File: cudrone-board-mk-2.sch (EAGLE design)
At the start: 144 parts, among them U1 EDISON_CONNECTOR_FULLMOUNTING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, U10 A2235-H, U11 FTS31XS-U, U12 BNO055, U13 DSPIC33EP512MU810-X_PF, U2 FTS31XS-U, U4 TPS62065, U5 USD-SOCKETNEW, U6 TXB0108, U8 PCA9306, U9 PCA9306

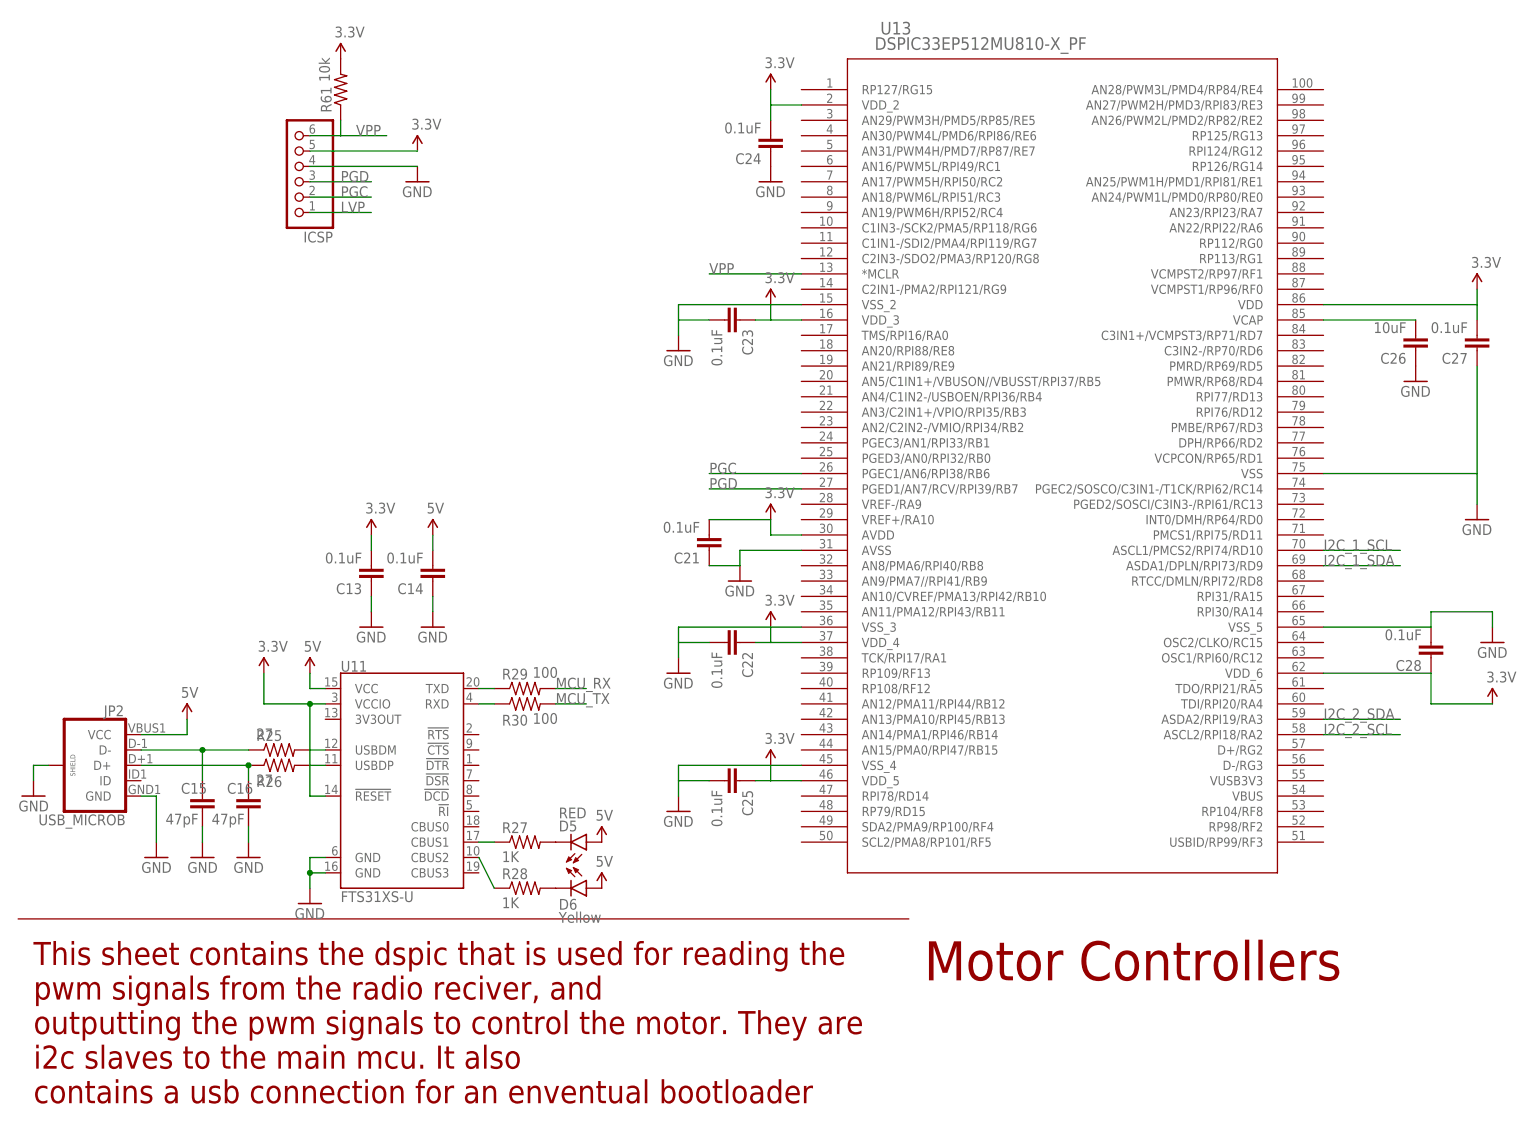
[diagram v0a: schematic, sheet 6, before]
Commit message: Made a few modifications in preparation of assigning pins on mcu
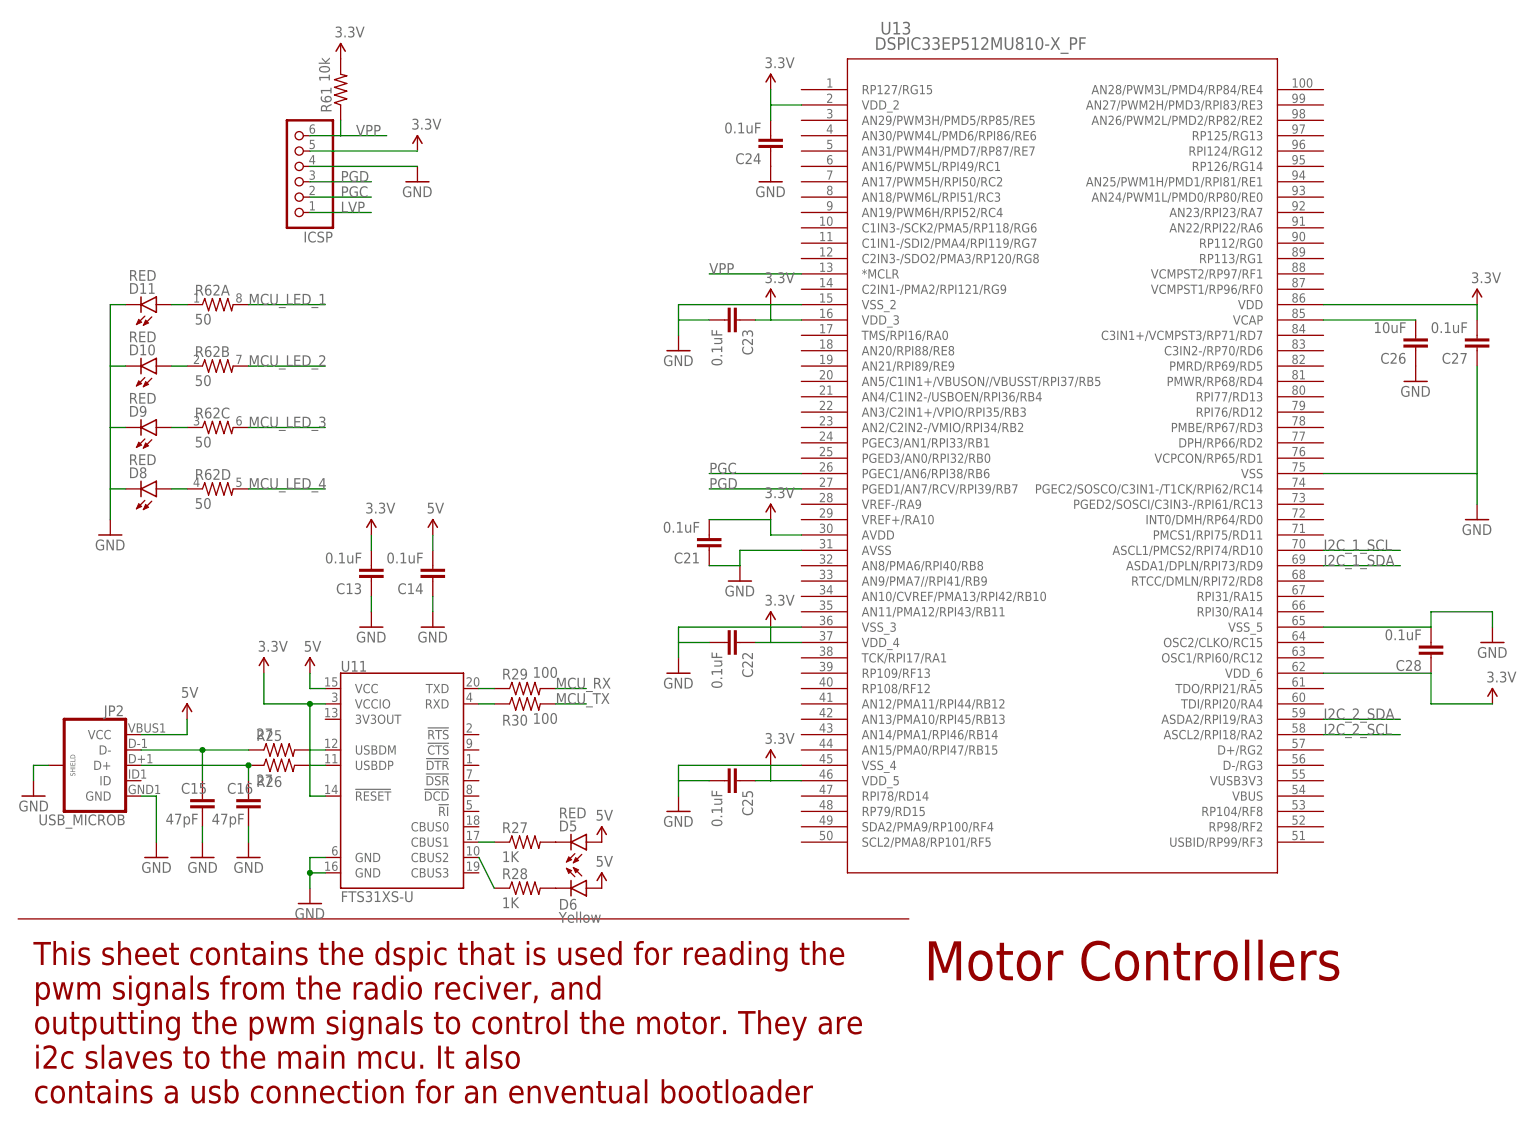
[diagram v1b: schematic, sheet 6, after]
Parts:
- added D10, D11, D8, D9: RED, SparkFun-LED:LED-RED0603
- added R62: 50, SparkFun-Passives:RESISTOR-ARRAY0603-ARV
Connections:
- new net MCU_LED_1: R62A.2
- new net MCU_LED_2: R62B.2
- new net MCU_LED_3: R62C.2
- new net MCU_LED_4: R62D.2
- new net N$13: D8.A, R62D.1
- new net N$33: D9.A, R62C.1
- new net N$43: D10.A, R62B.1
- new net N$44: D11.A, R62A.1
- net GND: now also D10.C, D11.C, D8.C, D9.C
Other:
- note added: "----LED----"
- note added: "MCU"
- note added: "Sensors"
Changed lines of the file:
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@@
 <part name="GND61" library="SparkFun-Aesthetics" deviceset="GND" device=""/>
 <part name="SUPPLY103" library="SparkFun-Aesthetics" deviceset="3.3V" device=""/>
+<part name="R62" library="SparkFun-Passives" deviceset="RESISTOR-ARRAY" device="0603-ARV" value="50"/>
+<part name="D8" library="SparkFun-LED" deviceset="LED-RED" device="0603" value="RED"/>
+<part name="D9" library="SparkFun-LED" deviceset="LED-RED" device="0603" value="RED"/>
+<part name="D10" library="SparkFun-LED" deviceset="LED-RED" device="0603" value="RED"/>
+<part name="D11" library="SparkFun-LED" deviceset="LED-RED" device="0603" value="RED"/>
+<part name="GND62" library="SparkFun-Aesthetics" deviceset="GND" device=""/>
 </parts>
 <sheets>
@@
 <text x="73.66" y="121.92" size="1.778" layer="97" rot="R270">---USB_OTG---</text>
 <text x="172.72" y="144.78" size="1.778" layer="97" rot="R270">----SD_CARD----</text>
-<text x="170.18" y="66.04" size="1.778" layer="97" rot="R270">--------I2C--------</text>
+<text x="170.18" y="63.5" size="1.778" layer="97" rot="R270">--------I2C--------</text>
 <text x="175.26" y="111.76" size="1.778" layer="97" rot="R90">GPS_UART</text>
+<text x="167.64" y="48.26" size="1.016" layer="97" rot="R90">Sensors</text>
+<text x="167.64" y="60.96" size="1.016" layer="97" rot="R90">MCU</text>
+<text x="86.36" y="78.74" size="1.778" layer="97" rot="R90">----LED----</text>
 </plain>
 <instances>
@@
 <instance part="C26" gate="G$1" x="231.14" y="132.08" rot="R180"/>
 <instance part="GND59" gate="1" x="231.14" y="124.46"/>
-<instance part="SUPPLY102" gate="G$1" x="241.3" y="139.7"/>
+<instance part="SUPPLY102" gate="G$1" x="241.3" y="137.16"/>
 <instance part="C27" gate="G$1" x="241.3" y="132.08" rot="R180"/>
 <instance part="GND60" gate="1" x="241.3" y="101.6"/>
@@
 <instance part="GND61" gate="1" x="243.84" y="81.28"/>
 <instance part="SUPPLY103" gate="G$1" x="243.84" y="71.12"/>
+<instance part="R62" gate="A" x="33.02" y="137.16"/>
+<instance part="R62" gate="B" x="33.02" y="127"/>
+<instance part="R62" gate="C" x="33.02" y="116.84"/>
+<instance part="R62" gate="D" x="33.02" y="106.68"/>
+<instance part="D8" gate="G$1" x="22.86" y="106.68" rot="MR90"/>
+<instance part="D9" gate="G$1" x="22.86" y="116.84" rot="MR90"/>
+<instance part="D10" gate="G$1" x="22.86" y="127" rot="MR90"/>
+<instance part="D11" gate="G$1" x="22.86" y="137.16" rot="MR90"/>
+<instance part="GND62" gate="1" x="15.24" y="99.06"/>
 </instances>
 <busses>
@@
 <pinref part="U13" gate="A" pin="VSS_5"/>
 <wire x1="233.68" y1="83.82" x2="215.9" y2="83.82" width="0.1524" layer="91"/>
+</segment>
+<segment>
+<pinref part="GND62" gate="1" pin="GND"/>
+<wire x1="15.24" y1="101.6" x2="15.24" y2="106.68" width="0.1524" layer="91"/>
+<pinref part="D11" gate="G$1" pin="C"/>
+<wire x1="15.24" y1="106.68" x2="15.24" y2="116.84" width="0.1524" layer="91"/>
+<wire x1="15.24" y1="116.84" x2="15.24" y2="127" width="0.1524" layer="91"/>
+<wire x1="15.24" y1="127" x2="15.24" y2="137.16" width="0.1524" layer="91"/>
+<wire x1="15.24" y1="137.16" x2="17.78" y2="137.16" width="0.1524" layer="91"/>
+<pinref part="D10" gate="G$1" pin="C"/>
+<wire x1="17.78" y1="127" x2="15.24" y2="127" width="0.1524" layer="91"/>
+<pinref part="D9" gate="G$1" pin="C"/>
+<wire x1="17.78" y1="116.84" x2="15.24" y2="116.84" width="0.1524" layer="91"/>
+<pinref part="D8" gate="G$1" pin="C"/>
+<wire x1="17.78" y1="106.68" x2="15.24" y2="106.68" width="0.1524" layer="91"/>
 </segment>
 </net>
@@
 <pinref part="SUPPLY102" gate="G$1" pin="3.3V"/>
 <pinref part="C27" gate="G$1" pin="2"/>
-<wire x1="241.3" y1="139.7" x2="241.3" y2="137.16" width="0.1524" layer="91"/>
 <pinref part="U13" gate="A" pin="VDD"/>
 <wire x1="241.3" y1="137.16" x2="241.3" y2="134.62" width="0.1524" layer="91"/>
@@
 <wire x1="215.9" y1="66.04" x2="228.6" y2="66.04" width="0.1524" layer="91"/>
 <label x="215.9" y="66.04" size="1.778" layer="95"/>
+</segment>
+</net>
+<net name="N$13" class="0">
+<segment>
+<pinref part="D8" gate="G$1" pin="A"/>
+<pinref part="R62" gate="D" pin="1"/>
+<wire x1="25.4" y1="106.68" x2="27.94" y2="106.68" width="0.1524" layer="91"/>
+</segment>
+</net>
+<net name="N$33" class="0">
+<segment>
+<pinref part="D9" gate="G$1" pin="A"/>
+<pinref part="R62" gate="C" pin="1"/>
+<wire x1="25.4" y1="116.84" x2="27.94" y2="116.84" width="0.1524" layer="91"/>
+</segment>
+</net>
+<net name="N$43" class="0">
+<segment>
+<pinref part="D10" gate="G$1" pin="A"/>
+<pinref part="R62" gate="B" pin="1"/>
+<wire x1="25.4" y1="127" x2="27.94" y2="127" width="0.1524" layer="91"/>
+</segment>
+</net>
+<net name="N$44" class="0">
+<segment>
+<pinref part="D11" gate="G$1" pin="A"/>
+<pinref part="R62" gate="A" pin="1"/>
+<wire x1="25.4" y1="137.16" x2="27.94" y2="137.16" width="0.1524" layer="91"/>
+</segment>
+</net>
+<net name="MCU_LED_1" class="0">
+<segment>
+<pinref part="R62" gate="A" pin="2"/>
+<wire x1="38.1" y1="137.16" x2="50.8" y2="137.16" width="0.1524" layer="91"/>
+<label x="38.1" y="137.16" size="1.778" layer="95"/>
+</segment>
+</net>
+<net name="MCU_LED_2" class="0">
+<segment>
+<pinref part="R62" gate="B" pin="2"/>
+<wire x1="38.1" y1="127" x2="50.8" y2="127" width="0.1524" layer="91"/>
+<label x="38.1" y="127" size="1.778" layer="95"/>
+</segment>
+</net>
+<net name="MCU_LED_3" class="0">
+<segment>
+<pinref part="R62" gate="C" pin="2"/>
+<wire x1="38.1" y1="116.84" x2="50.8" y2="116.84" width="0.1524" layer="91"/>
+<label x="38.1" y="116.84" size="1.778" layer="95"/>
+</segment>
+</net>
+<net name="MCU_LED_4" class="0">
+<segment>
+<pinref part="R62" gate="D" pin="2"/>
+<wire x1="38.1" y1="106.68" x2="50.8" y2="106.68" width="0.1524" layer="91"/>
+<label x="38.1" y="106.68" size="1.778" layer="95"/>
 </segment>
 </net>
@@
  and landing gear, the connections to the reciver
 and the connections to the esc</text>
-<text x="137.16" y="78.74" size="1.778" layer="91">MCU is running at 3.3V so pullups to make output signal at 5V and the mcu is pulling down.</text>
+<text x="137.16" y="78.74" size="1.778" layer="97">MCU is running at 3.3V so pullups to make output signal at 5V and the mcu is pulling down.</text>
 </plain>
 <instances>

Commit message: Added a bunch of tank capacitors
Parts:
- added C29: 0.1uF, SparkFun-Capacitors:0.1UF-25V(+80/-20%)(0603)
- added C30, C31, C32, C33, C34, C35, C36, C37, C38, C39, C40, C41, C42, C43, C44, C45, C46: 47 uF, SparkFun-Passives:CAP0805
- C6: value 22uF -> 47 uF; device SparkFun-Capacitors:22UF-6.3V-20%(0805) -> SparkFun-Passives:CAP0805
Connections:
- net 3.3V: now also C29.2, C30.1, C31.1, C32.1, C33.1, C34.1, C35.1, C36.1, C37.1, C38.1, C39.1, C40.1, C41.1, C42.1, C43.1, C44.1, C45.1, C46.1, U13.VUSB3V3
- net GND: now also C29.1, C30.2, C31.2, C32.2, C33.2, C34.2, C35.2, C36.2, C37.2, C38.2, C39.2, C40.2, C41.2, C42.2, C43.2, C44.2, C45.2, C46.2
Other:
- note added: "Tank Capacitors, 2 per power pin"
- note added: "Tank Capacitors, one on each side"
- moved on the sheet: C6, D3, R5

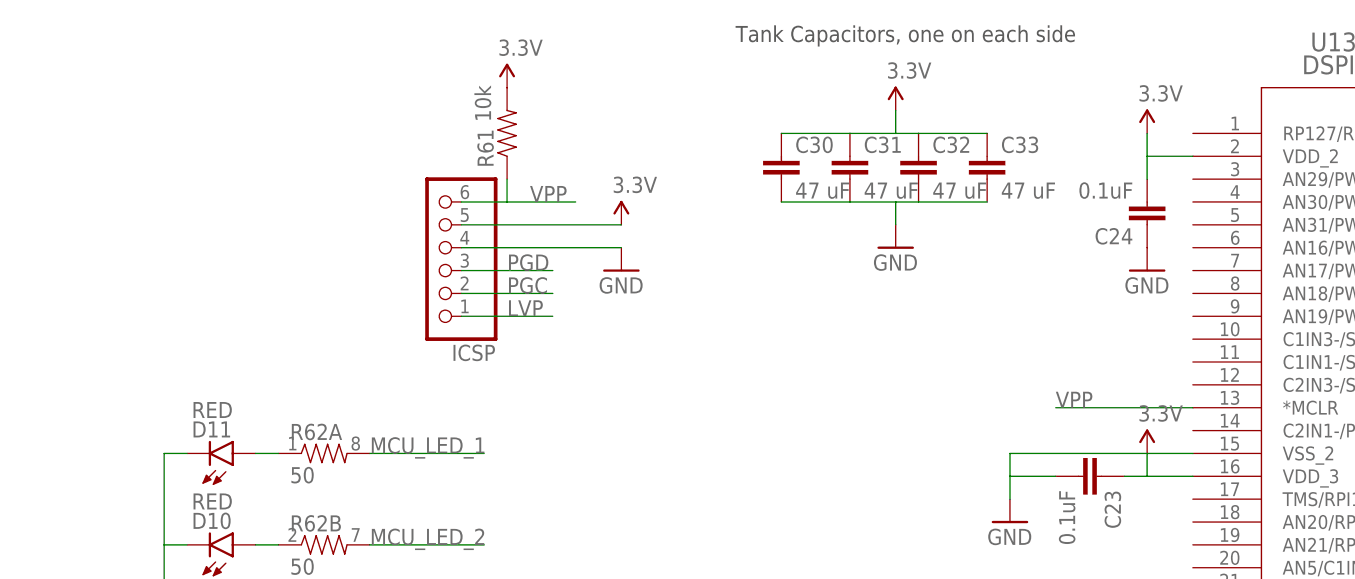
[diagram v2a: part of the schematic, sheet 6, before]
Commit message: Added reset to mcu
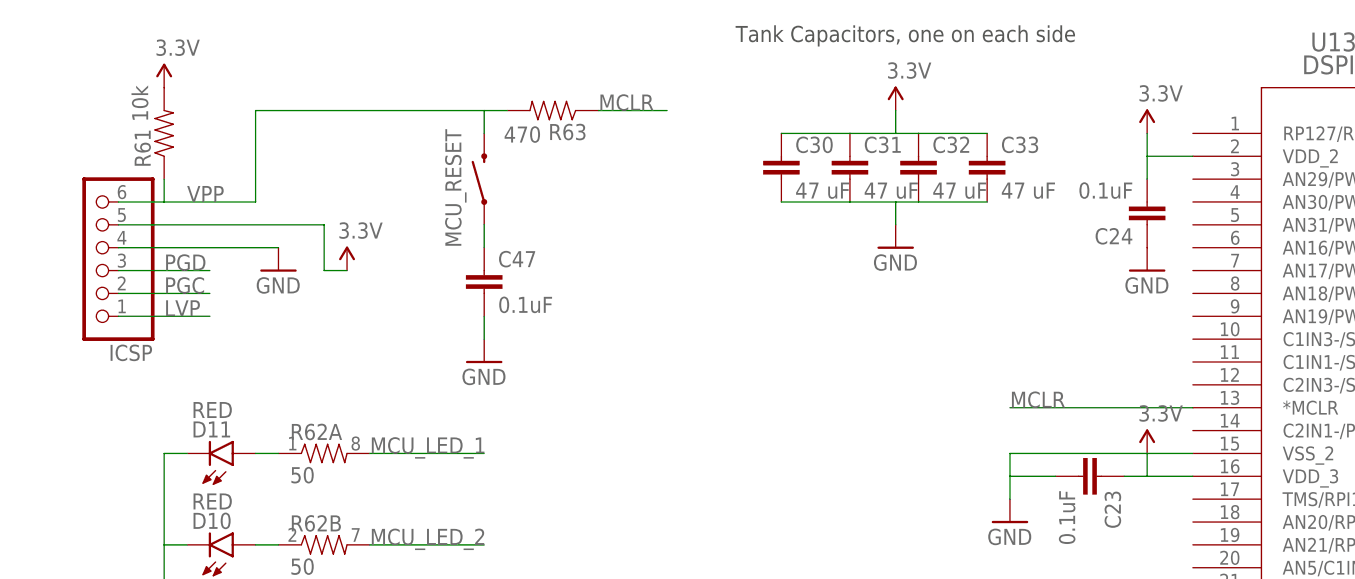
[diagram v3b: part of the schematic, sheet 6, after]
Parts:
- removed RESET: SWITCH-MOMENTARY-2PTH, SparkFun-Electromechanical:SWITCH-MOMENTARY-2PTH
- added C47: 0.1uF, SparkFun-Capacitors:0.1UF-25V(+80/-20%)(0603)
- added EDISON_RESET, MCU_RESET: SWITCH-MOMENTARY-2, SparkFun-Electromechanical:SWITCH-MOMENTARY-2
- added R63: 470, SparkFun-Resistors:27OHM1/10W1%(0603)
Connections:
- new net MCLR: R63.1, U13.*MCLR
- new net N$45: C47.1, MCU_RESET.1
- net GND: now also C47.2, EDISON_RESET.2; no longer RESET.2
- net N$15: now also EDISON_RESET.1; no longer RESET.1
- net VPP: now also MCU_RESET.2, R63.2; no longer U13.*MCLR
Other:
- moved on the sheet: ICSP, R61
